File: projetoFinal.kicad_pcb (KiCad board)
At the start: 2 copper layers, 27 parts, among them J1 Conn_01x01_Male, J3 Conn_01x01_Male, J4 Conn_01x01_Male, J5 Conn_01x01_Male, U1 LM317_TO-220, U2 LM337_TO220

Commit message: roteamento feito
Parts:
- added HS1: Heatsink, Heatsink:Heatsink_Stonecold_HS-132_32x14mm_2xFixation1.5mm, F.Cu at (104.1, 161.3)
- added HS2: Heatsink, Heatsink:Heatsink_Stonecold_HS-132_32x14mm_2xFixation1.5mm, F.Cu at (102.9, 50.8)
- added J2: Conn_01x04, TerminalBlock_Phoenix:TerminalBlock_Phoenix_MKDS-3-4-5.08_1x04_P5.08mm_Horizontal, F.Cu at (51.8, 94.0)
- added J6: Conn_01x04, Connector_PinHeader_2.54mm:PinHeader_1x04_P2.54mm_Vertical, F.Cu at (149.9, 132.1)
- C1, C9: footprint Capacitor_THT:CP_Radial_Tantal_D6.0mm_P5.00mm -> Capacitor_THT:CP_Radial_D10.0mm_P2.50mm
- C10, C2, C4, C8: footprint Capacitor_THT:C_Axial_L3.8mm_D2.6mm_P7.50mm_Horizontal -> Capacitor_THT:C_Disc_D3.0mm_W2.0mm_P2.50mm
- C3, C7: footprint Capacitor_THT:C_Axial_L3.8mm_D2.6mm_P7.50mm_Horizontal -> Capacitor_THT:CP_Radial_D7.5mm_P2.50mm
- C5, C6: footprint Capacitor_THT:C_Axial_L3.8mm_D2.6mm_P7.50mm_Horizontal -> Capacitor_THT:CP_Radial_D5.0mm_P2.50mm
- D1, D2, D4, D5: footprint Diode_THT:D_A-405_P10.16mm_Horizontal -> Diode_THT:D_5W_P10.16mm_Horizontal
- D6: footprint Diode_THT:D_A-405_P10.16mm_Horizontal -> LED_THT:LED_D5.0mm
- J1, J3, J4, J5: footprint MountingHole:MountingHole_2.2mm_M2_DIN965_Pad -> footprints:Banana_Jack_1Pin
- R1, R2: footprint Resistor_THT:R_Axial_DIN0204_L3.6mm_D1.6mm_P7.62mm_Horizontal -> Resistor_THT:R_Axial_DIN0207_L6.3mm_D2.5mm_P10.16mm_Horizontal
- moved D6 132.3 mm to (62.2, 142.2), turned to 90 degrees
- moved D1 105.2 mm to (99.1, 141.0)
- moved C1 92.6 mm to (74.9, 127.0), turned to -90 degrees
- moved R3 89.8 mm to (62.2, 127.0), turned to -90 degrees
- moved D2 83.4 mm to (129.5, 127.0), turned to -90 degrees
- moved J1 81.9 mm to (172.7, 141.0)
- moved C9 80.2 mm to (74.9, 71.1), turned to -90 degrees
- moved C10 77.2 mm to (85.1, 71.2), turned to -90 degrees
- moved C2 76.4 mm to (88.9, 127.0), turned to -90 degrees
- moved U1 72.3 mm to (106.7, 157.5), turned to 180 degrees
- moved C5 70.3 mm to (129.5, 113.0), turned to 90 degrees
- moved C4 66.6 mm to (152.4, 113.0), turned to 90 degrees
- moved J3 66.2 mm to (172.7, 118.1)
- moved RV1 63.3 mm to (99.1, 109.7), turned to -90 degrees
- moved R1 60.1 mm to (120.7, 127.0), turned to -90 degrees
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
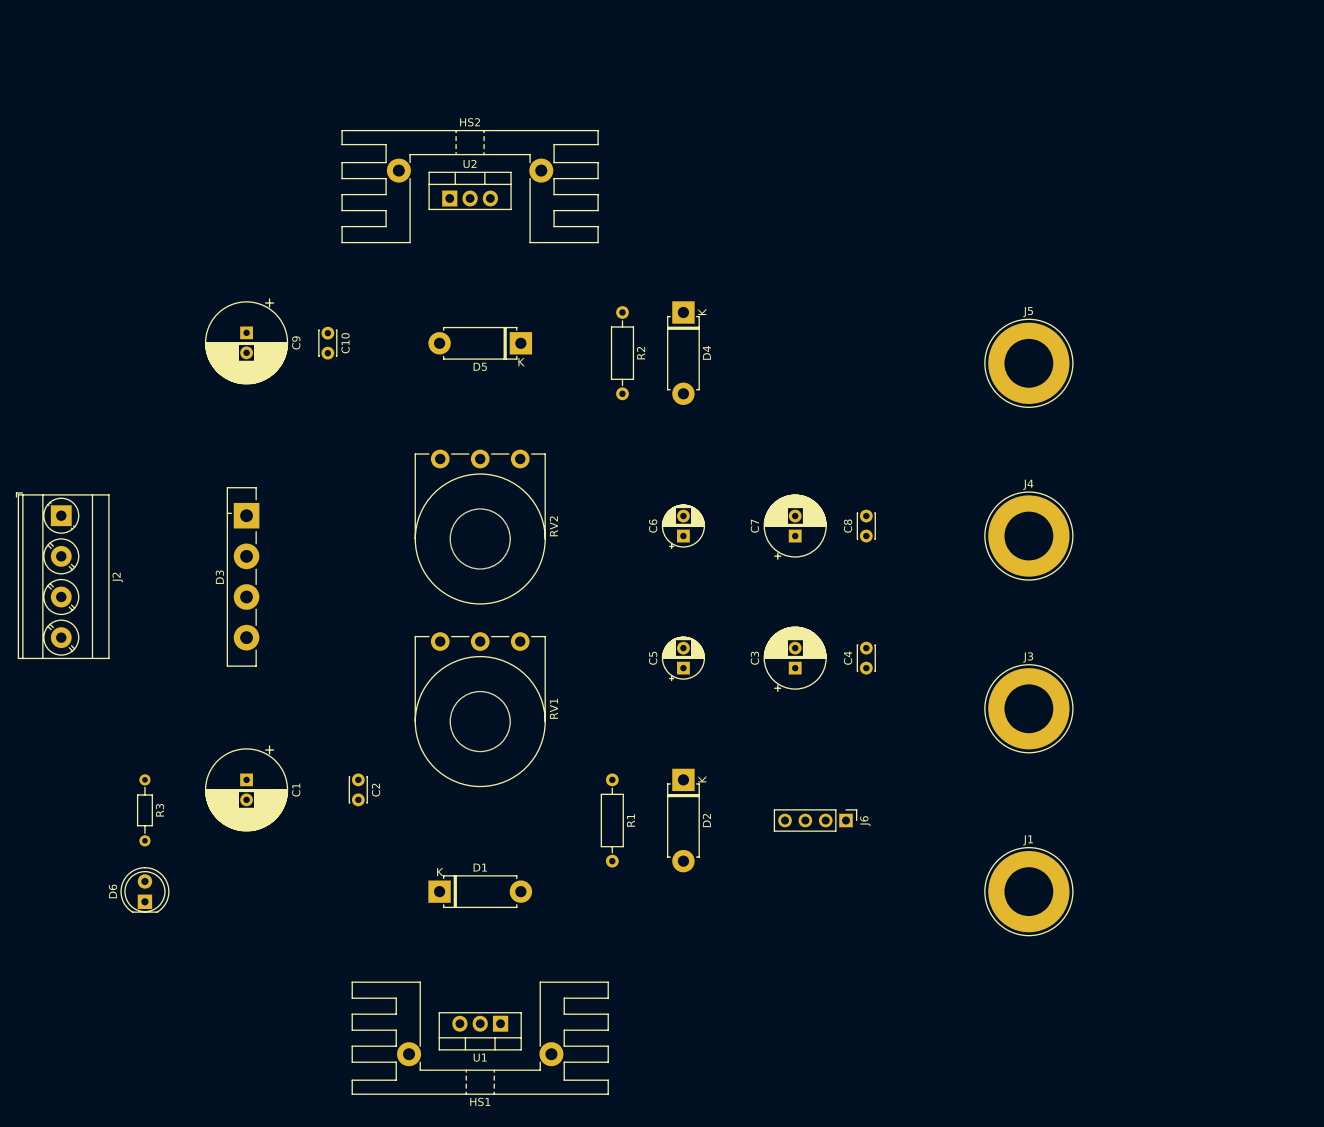
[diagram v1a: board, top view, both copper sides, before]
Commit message: novo roteamento da placa
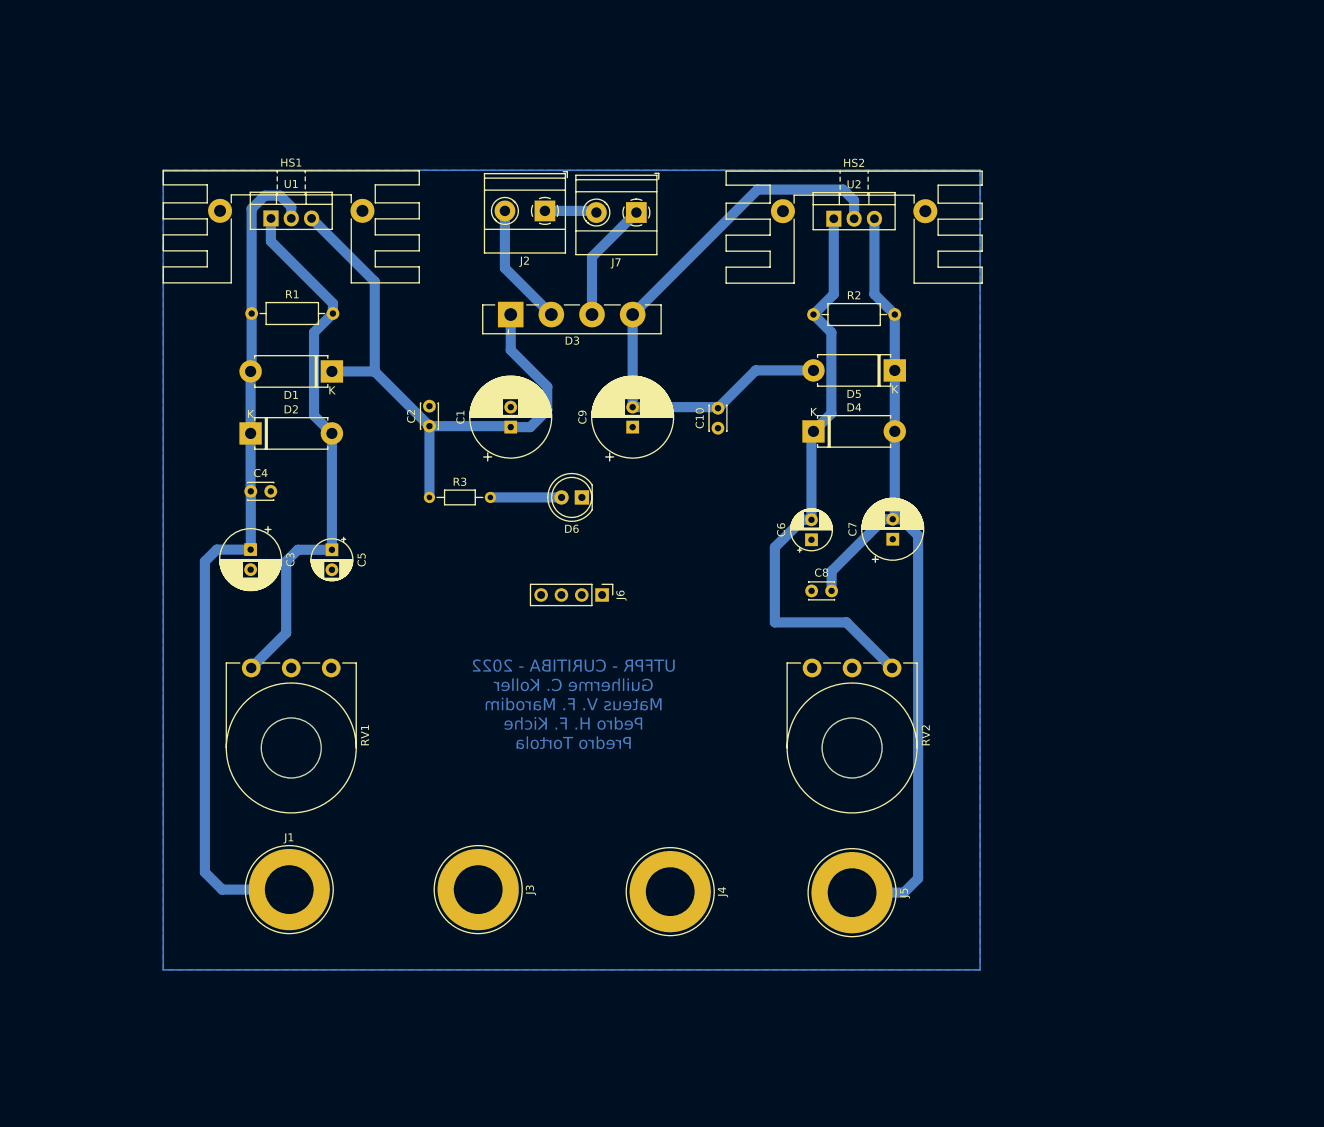
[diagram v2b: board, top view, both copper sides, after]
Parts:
- added J7: Conn_01x02, TerminalBlock_Phoenix:TerminalBlock_Phoenix_MKDS-1,5-2_1x02_P5.00mm_Horizontal, F.Cu at (123.7, 56.1)
- J2: value Conn_01x04 -> Conn_01x02; footprint TerminalBlock_Phoenix:TerminalBlock_Phoenix_MKDS-3-4-5.08_1x04_P5.08mm_Horizontal -> TerminalBlock_Phoenix:TerminalBlock_Phoenix_MKDS-1,5-2_1x02_P5.00mm_Horizontal
- moved HS1 108.0 mm to (80.5, 55.9), turned to 0 degrees
- moved U1 104.7 mm to (78.0, 56.8), turned to 0 degrees
- moved J1 92.5 mm to (80.3, 140.7)
- moved C4 80.1 mm to (75.5, 90.9), turned to 0 degrees
- moved D6 74.4 mm to (116.8, 91.7), turned to 180 degrees
- moved R1 73.7 mm to (75.6, 68.7), turned to 0 degrees
- moved J3 72.5 mm to (103.9, 140.7), turned to -90 degrees
- moved J2 71.5 mm to (112.2, 55.9), turned to 180 degrees
- moved J5 69.8 mm to (150.6, 141.1), turned to -90 degrees
- moved C3 69.7 mm to (75.4, 98.2), turned to -90 degrees
- moved D2 69.3 mm to (75.4, 83.7), turned to 0 degrees
- moved D1 66.4 mm to (85.6, 75.9), turned to 180 degrees
- moved J4 63.1 mm to (127.9, 141.0), turned to -90 degrees
- moved C1 55.1 mm to (108.0, 82.9), turned to 90 degrees
- moved RV2 53.3 mm to (145.6, 113.0)
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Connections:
- J2 pad 1: Net-(D3-Pad2) -> GND
- J2 pad 2: GND -> Net-(D3-Pad2)
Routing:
- net Net-(C7-Pad2): track 0.00 -> 107.4 mm
- net Net-(C3-Pad1): track 0.00 -> 107.0 mm
- net Net-(C1-Pad1): track 0.00 -> 75.8 mm
- net Net-(C10-Pad2): track 0.00 -> 73.2 mm
- net Net-(D4-Pad1): track 0.00 -> 73.0 mm
- net Net-(C5-Pad1): track 0.00 -> 68.0 mm
- net Net-(D3-Pad2): track 0.00 -> 15.4 mm
- net Net-(D3-Pad3): track 0.00 -> 15.0 mm
- net Net-(D6-Pad2): track 0.00 -> 8.90 mm
- net GND: track 0.00 -> 6.51 mm
- added copper zone on B.Cu, net GND
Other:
- board text added: "UTFPR - CURITIBA - 2022 Guilherme C. Koller Mateus V. F. Marodim Pedro H. F. Kiche Predro Tortola"

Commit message: layout final
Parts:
- C1, C9: footprint Capacitor_THT:CP_Radial_D10.0mm_P2.50mm -> Capacitor_THT:CP_Radial_D12.5mm_P5.00mm
- moved J6 7.61 mm to (111.8, 103.6), turned to 90 degrees
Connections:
- J6 pad 1: /V+ -> Net-(C3-Pad1)
- J6 pad 4: /V- -> Net-(C7-Pad2)
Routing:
- net Net-(C7-Pad2): track 107.4 -> 165.9 mm
- net Net-(C3-Pad1): track 107.0 -> 163.3 mm
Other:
- board text added: "UTFPR - CURITIBA - 2022 Guilherme C. Koller Mateus V. F. Marodim Pedro H. F. Kiche Pedro A. Tortola P."
- board text removed: "UTFPR - CURITIBA - 2022 Guilherme C. Koller Mateus V. F. Marodim Pedro H. F. Kiche Predro Tortola"

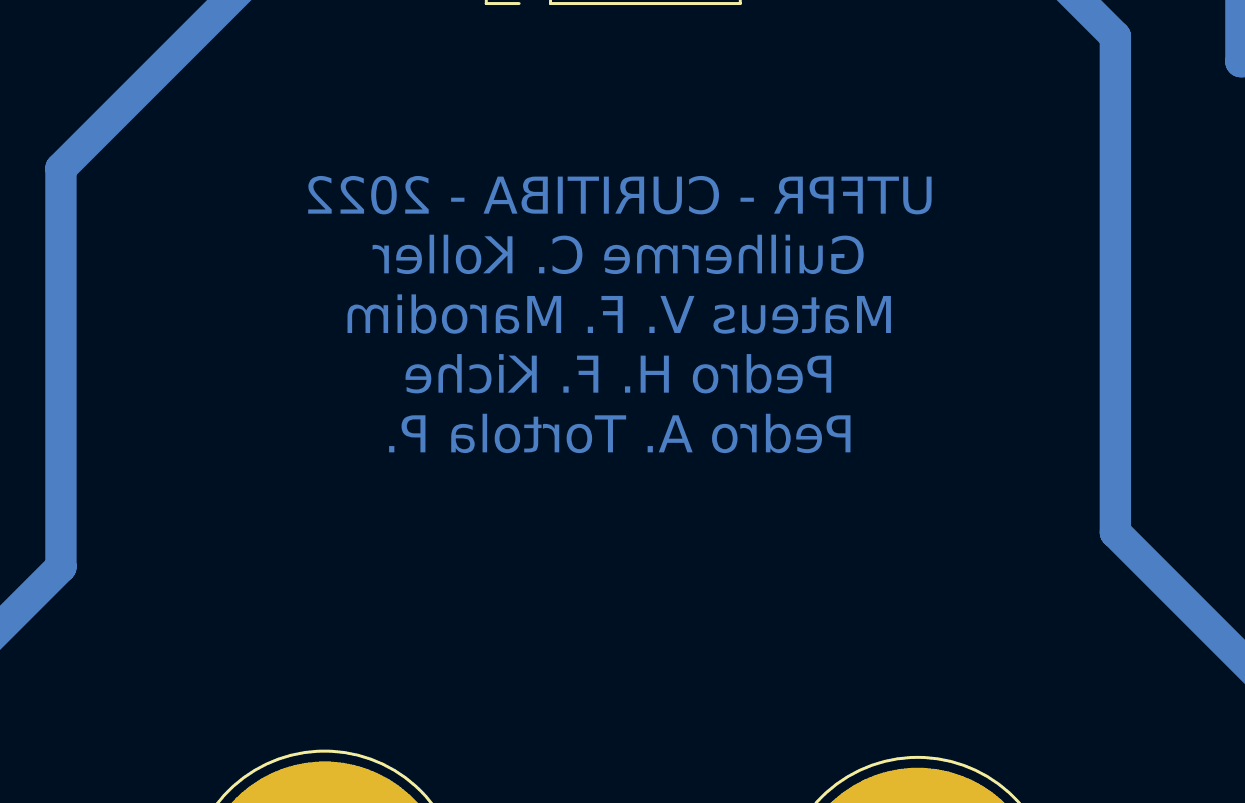
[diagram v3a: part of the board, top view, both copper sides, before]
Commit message: fonte dos nomes aumentada
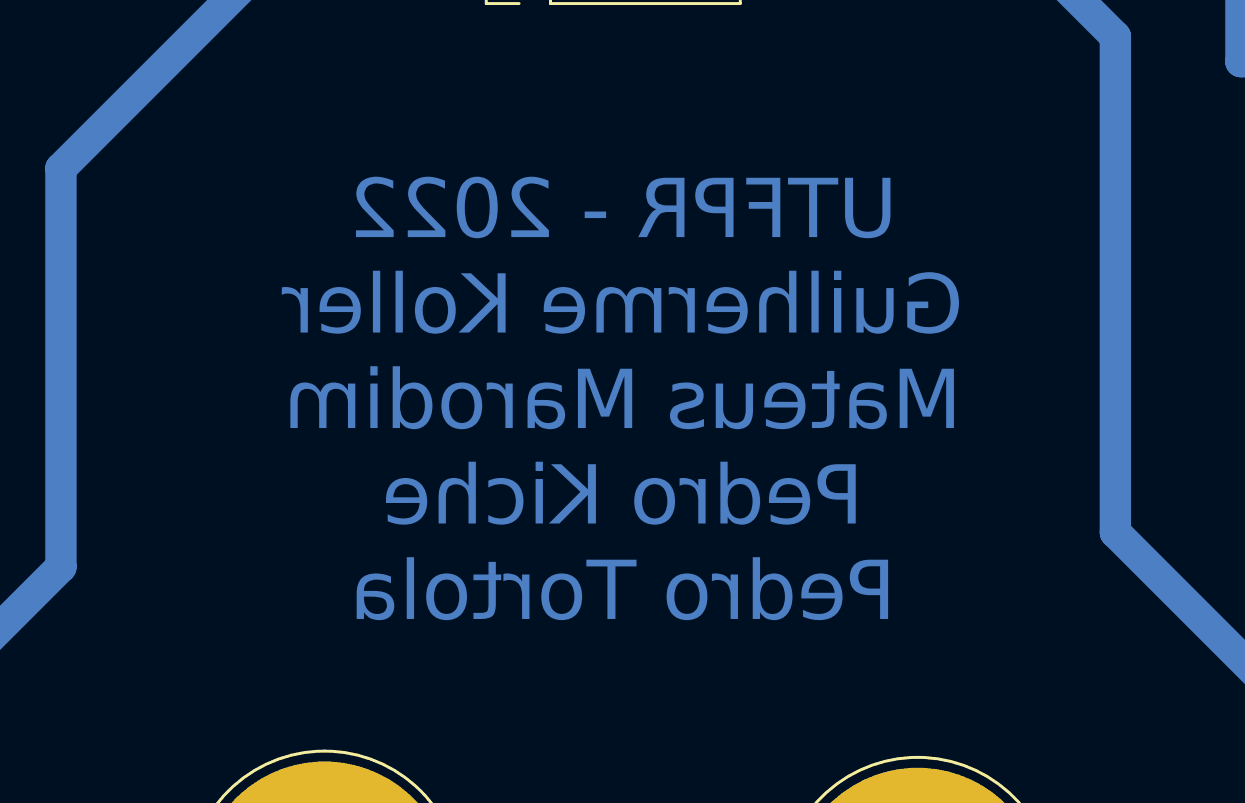
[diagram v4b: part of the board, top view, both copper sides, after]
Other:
- board text added: "UTFPR - 2022 Guilherme Koller Mateus Marodim Pedro Kiche Pedro Tortola"
- board text removed: "UTFPR - CURITIBA - 2022 Guilherme C. Koller Mateus V. F. Marodim Pedro H. F. Kiche Pedro A. Tortola P."
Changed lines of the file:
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@@
   )
   (gr_rect (start 64.516 50.8) (end 166.624 150.749) (layer "B.Cu") (width 0.2) (fill none))
-  (gr_text "UTFPR - CURITIBA - 2022\nGuilherme C. Koller\nMateus V. F. Marodim\nPedro H. F. Kiche\nPedro A. Tortola P." (at 115.824 117.602) (layer "B.Cu")
-    (effects (font (size 1.5 1.5) (thickness 0.3)) (justify mirror))
+  (gr_text "UTFPR - 2022\nGuilherme Koller\nMateus Marodim\nPedro Kiche\nPedro Tortola" (at 115.951 121.031) (layer "B.Cu")
+    (effects (font (size 2.4 2.4) (thickness 0.5)) (justify mirror))
   )
   (segment (start 97.79 82.784) (end 107.828323 82.784) (width 1.27) (layer "B.Cu") (net 1))

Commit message: correção final na placa
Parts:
- moved J1 12.4 mm to (80.1, 153.2)
- moved J3 12.4 mm to (103.8, 153.2)
- moved J4 12.4 mm to (127.8, 153.4)
- moved J5 12.4 mm to (150.5, 153.5)
- moved RV1 7.64 mm to (75.4, 120.7)
- moved RV2 7.64 mm to (145.5, 120.7)
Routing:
- net GND: track 6.51 -> 31.5 mm
- net Net-(C7-Pad2): track 165.9 -> 188.1 mm
- net Net-(C3-Pad1): track 163.3 -> 184.1 mm
- net Net-(C6-Pad2): track 73.0 -> 81.4 mm
- net Net-(C5-Pad1): track 68.0 -> 75.6 mm
